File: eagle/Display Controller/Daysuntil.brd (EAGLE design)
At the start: 45 parts, among them IC1 DS1307, IC2 ATMEGA168-20P, IC3 74HC595N, IC4 74HC595N, IC5 7805TV, Q1 32.768 kHz, T1 BC337, T10 BC337, T11 BC337, T12 BC337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

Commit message: updated board config
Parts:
- C1, C4, C5, C6: value 10uF -> 0.1uF
- C2, C3: value 10uF -> 100uF
- U$2: value (none) -> 16MHz
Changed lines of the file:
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@@
 <attribute name="VALUE" x="66.9798" y="40.132" size="1.778" layer="27" ratio="10" rot="R90"/>
 </element>
-<element name="U$2" library="adafruit" package="CERM_OSC" value="" x="46.99" y="33.02" smashed="yes" rot="R180">
+<element name="U$2" library="adafruit" package="CERM_OSC" value="16MHz" x="46.99" y="33.02" smashed="yes" rot="R180">
 <attribute name="VALUE" x="50.49" y="37.52" size="1.27" layer="27" rot="R180"/>
 </element>
@@
 <attribute name="VALUE" x="27.94" y="26.67" size="1.27" layer="27" ratio="10" rot="R90"/>
 </element>
-<element name="C2" library="adafruit" package="C050-050X075" value="10uF" x="22.86" y="27.94" smashed="yes" rot="R270">
+<element name="C2" library="adafruit" package="C050-050X075" value="100uF" x="22.86" y="27.94" smashed="yes" rot="R270">
 <attribute name="NAME" x="22.479" y="23.749" size="1.27" layer="25" ratio="10" rot="R180"/>
 <attribute name="VALUE" x="20.701" y="31.115" size="1.27" layer="27" ratio="10" rot="R270"/>
 </element>
-<element name="C3" library="adafruit" package="C050-050X075" value="10uF" x="36.83" y="31.75" smashed="yes" rot="R90">
+<element name="C3" library="adafruit" package="C050-050X075" value="100uF" x="36.83" y="31.75" smashed="yes" rot="R90">
 <attribute name="NAME" x="37.719" y="27.559" size="1.27" layer="25" ratio="10" rot="R180"/>
 <attribute name="VALUE" x="38.989" y="28.575" size="1.27" layer="27" ratio="10" rot="R90"/>
 </element>
 <element name="JP1" library="pinhead" package="1X16" value="Output" x="17.78" y="46.99" rot="R270"/>
-<element name="C1" library="adafruit" package="C025-030X050" value="10uF" x="67.31" y="68.58" smashed="yes">
+<element name="C1" library="adafruit" package="C025-030X050" value="0.1uF" x="67.31" y="68.58" smashed="yes">
 <attribute name="NAME" x="66.294" y="70.485" size="1.27" layer="25" ratio="10"/>
 <attribute name="VALUE" x="65.024" y="65.532" size="1.27" layer="27" ratio="10"/>
 </element>
-<element name="C4" library="adafruit" package="C025-030X050" value="10uF" x="40.64" y="24.13" smashed="yes" rot="R270">
+<element name="C4" library="adafruit" package="C025-030X050" value="0.1uF" x="40.64" y="24.13" smashed="yes" rot="R270">
 <attribute name="NAME" x="39.624" y="27.305" size="1.27" layer="25" ratio="10"/>
 <attribute name="VALUE" x="38.354" y="19.812" size="1.27" layer="27" ratio="10"/>
 </element>
-<element name="C6" library="adafruit" package="C025-030X050" value="10uF" x="35.56" y="52.07" smashed="yes" rot="R90">
+<element name="C6" library="adafruit" package="C025-030X050" value="0.1uF" x="35.56" y="52.07" smashed="yes" rot="R90">
 <attribute name="NAME" x="38.735" y="48.514" size="1.27" layer="25" ratio="10" rot="R90"/>
 <attribute name="VALUE" x="38.608" y="52.324" size="1.27" layer="27" ratio="10" rot="R90"/>
 </element>
-<element name="C5" library="adafruit" package="C025-030X050" value="10uF" x="35.56" y="40.64" smashed="yes" rot="R90">
+<element name="C5" library="adafruit" package="C025-030X050" value="0.1uF" x="35.56" y="40.64" smashed="yes" rot="R90">
 <attribute name="NAME" x="38.735" y="37.084" size="1.27" layer="25" ratio="10" rot="R90"/>
 <attribute name="VALUE" x="38.608" y="40.894" size="1.27" layer="27" ratio="10" rot="R90"/>

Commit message: finalized board design
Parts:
- added SL1: (no value), con-amp-quick:02P
- IC2: value ATMEGA168-20P -> ATMEGA328P
- JP1: value Output -> (none); device pinhead:1X16 -> pinhead:1X14
- moved C1 66.2 mm to (40.0, 8.26), turned to 270 degrees
- moved IC2 60.8 mm to (19.7, 6.35), turned to 180 degrees
- moved R9 57.3 mm to (14.0, 31.1), turned to 180 degrees
- moved R8 52.0 mm to (14.0, 34.9), turned to 180 degrees
- moved R7 46.6 mm to (14.0, 38.7), turned to 180 degrees
- moved R6 41.3 mm to (14.0, 42.5), turned to 180 degrees
- moved R16 36.1 mm to (38.1, 31.1), turned to 180 degrees
- moved T6 36.0 mm to (8.26, 28.9), turned to 0 degrees
- moved R5 35.9 mm to (14.0, 46.4), turned to 180 degrees
- moved T4 32.6 mm to (8.26, 38.4), turned to 0 degrees
- moved T7 31.0 mm to (8.26, 25.4)
- moved R15 30.8 mm to (38.1, 34.9), turned to 180 degrees
- moved R4 30.6 mm to (14.0, 50.2), turned to 180 degrees
- moved T2 29.5 mm to (8.26, 47.9), turned to 0 degrees
- moved IC3 27.9 mm to (23.5, 41.9), turned to 270 degrees
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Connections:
- net +12V: now also SL1.2; no longer JP1.16
- net GND: now also SL1.1; no longer JP1.15
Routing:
- net N$7: track 0.00 -> 72.0 mm, vias 0 -> 1
- net N$6: track 0.00 -> 68.2 mm, vias 0 -> 1
- net N$2: track 0.00 -> 56.5 mm, vias 0 -> 1
- net 9: track 0.00 -> 55.1 mm, vias 0 -> 1
- net 8: track 0.00 -> 52.8 mm
- net 10: track 0.00 -> 49.1 mm
- net N$9: track 0.00 -> 48.7 mm, vias 0 -> 1
- net SER: track 0.00 -> 45.8 mm
- net 12: track 0.00 -> 42.1 mm, vias 0 -> 1
- net N$8: track 0.00 -> 41.0 mm
- net 11: track 0.00 -> 39.2 mm, vias 0 -> 1
- net 14: track 0.00 -> 33.7 mm
- net 13: track 0.00 -> 32.6 mm
- net SCL: track 0.00 -> 30.7 mm, vias 0 -> 1
- net SDA: track 0.00 -> 30.1 mm
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- added copper zone on layer 1, net GND
- added copper zone on layer 16, net VCC
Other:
- board outline added: 56.5 x 59.7 mm
- board text added: "/home/brian/Pictures/Images/santa1.bmp"
- board text added: "1"
- board text added: "RTC Display v1.0"
- board text added: "wilsonb@outlook.com"
- board text removed: "2.2K"
- board text removed: "4.7K"
- board text removed: "BC337"

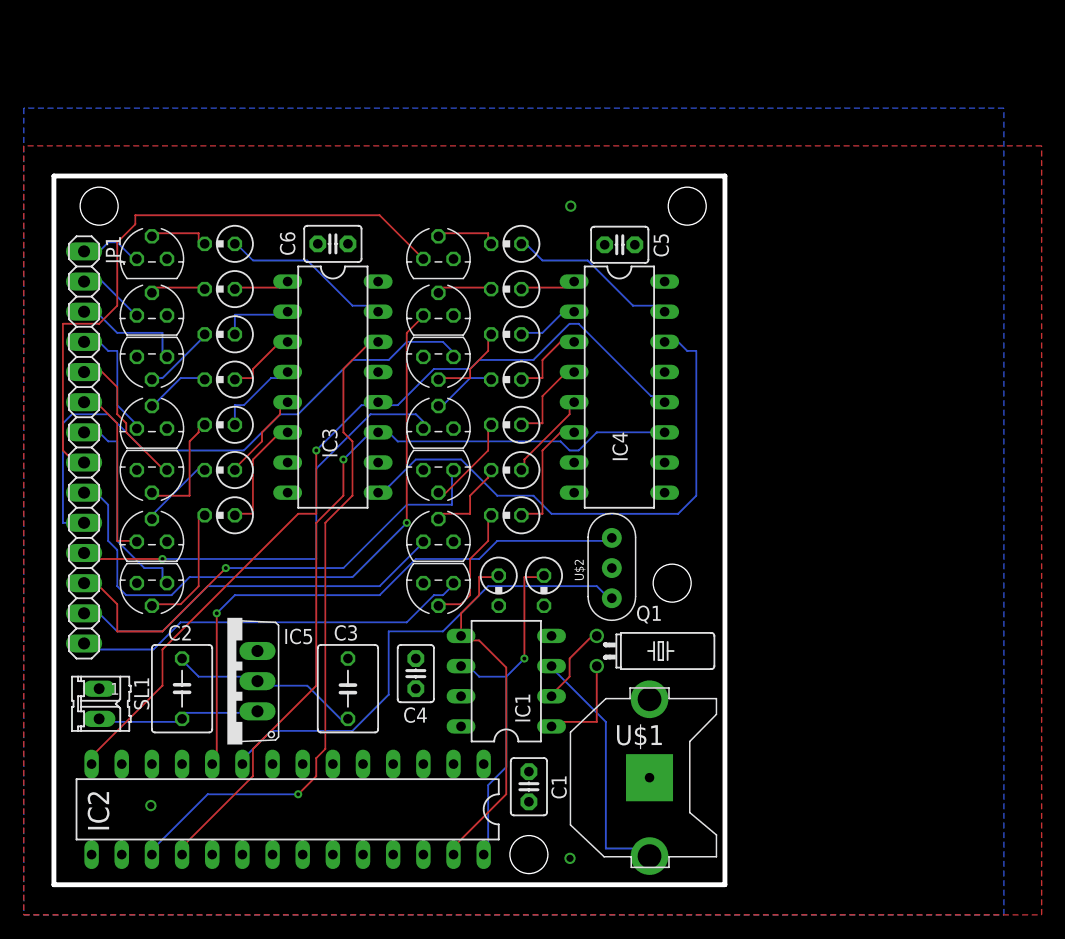
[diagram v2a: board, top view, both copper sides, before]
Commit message: final board design with CAM files
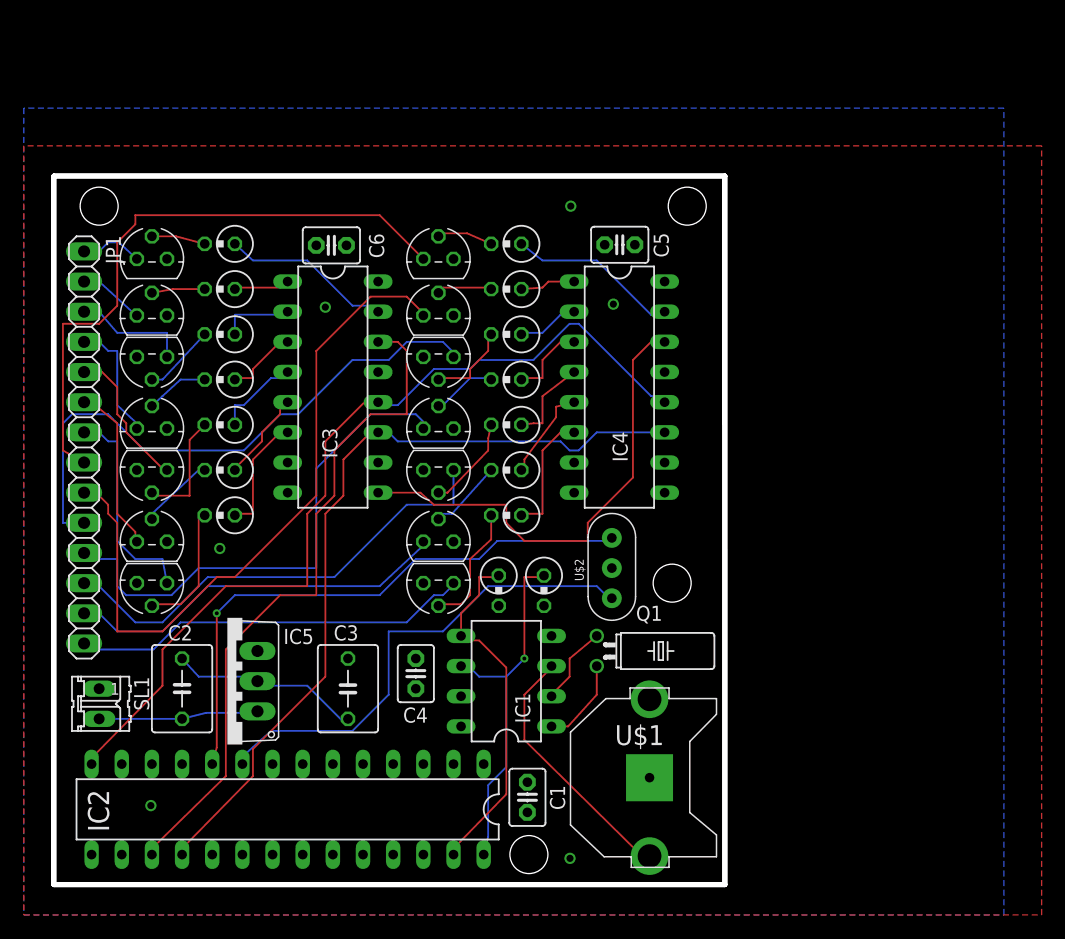
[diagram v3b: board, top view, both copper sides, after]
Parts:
- added U$3: (no value), bitmap:BITMAP-SLEIGHT
- moved C1 0.90 mm to (39.9, 7.37)
- moved C6 0.18 mm to (23.4, 53.8), turned to 180 degrees
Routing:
- net SER: track 45.8 -> 40.3 mm
- net 11: track 39.2 -> 43.5 mm, vias 1 -> 0
- net 9: track 55.1 -> 59.4 mm, vias 1 -> 0
- net N$7: track 72.0 -> 75.4 mm, vias 1 -> 0
- net 12: track 42.1 -> 39.5 mm, vias 1 -> 0
- net N$4: track 8.89 -> 7.41 mm
- net 6: track 15.5 -> 14.1 mm
- net N$21: track 7.60 -> 6.29 mm
- net N$2: track 56.5 -> 57.6 mm, vias 1 -> 0
- net +12V: track 14.4 -> 13.4 mm
- net N$1: track 5.38 -> 4.53 mm
- net 8: track 52.8 -> 52.1 mm
- net N$5: track 7.42 -> 6.78 mm
- net N$16: track 5.31 -> 4.71 mm
- net N$20: track 8.42 -> 7.89 mm
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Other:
- board text removed: "/home/brian/Pictures/Images/santa1.bmp"

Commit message: upload code v1 and fix ground on 7805 in board schematic.
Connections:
- removed net N$23: C2.2, C3.2, IC5.2
- net GND: now also C2.2, C3.2, IC5.2
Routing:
- net N$23: track 16.3 -> 0.00 mm
- net GND: track 0.00 -> 16.3 mm
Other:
- board text added: "RTC Display v1.1"
- board text removed: "RTC Display v1.0"
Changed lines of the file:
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@@
 <wire x1="56.515" y1="59.69" x2="56.515" y2="0" width="0.4064" layer="20"/>
 <hole x="3.81" y="57.15" drill="3.2"/>
-<text x="16.4338" y="56.5277" size="1.778" layer="121" font="vector">RTC Display v1.0</text>
+<text x="16.4338" y="56.5277" size="1.778" layer="121" font="vector">RTC Display v1.1</text>
 <text x="55.3212" y="27.305" size="1.778" layer="121" font="vector" rot="R90">wilsonb@outlook.com</text>
 <wire x1="0" y1="0" x2="0" y2="59.69" width="0.4064" layer="20"/>
@@
 <vertex x="83.185" y="62.23"/>
 </polygon>
+<contactref element="C2" pad="2"/>
+<contactref element="IC5" pad="2"/>
+<contactref element="C3" pad="2"/>
+<wire x1="12.192" y1="17.526" x2="10.795" y2="19.05" width="0.1524" layer="16"/>
+<wire x1="16.764" y1="17.526" x2="12.192" y2="17.526" width="0.1524" layer="16"/>
+<wire x1="16.764" y1="17.526" x2="17.145" y2="17.145" width="0.1524" layer="16"/>
+<wire x1="21.336" y1="16.764" x2="24.384" y2="13.716" width="0.1524" layer="16"/>
+<wire x1="17.526" y1="16.764" x2="21.336" y2="16.764" width="0.1524" layer="16"/>
+<wire x1="24.384" y1="13.716" x2="24.765" y2="13.97" width="0.1524" layer="16"/>
+<wire x1="17.526" y1="16.764" x2="17.145" y2="17.145" width="0.1524" layer="16"/>
 </signal>
 <signal name="VCC">
@@
 <wire x1="10.795" y1="13.97" x2="3.81" y2="13.97" width="0.1524" layer="16"/>
 </signal>
-<signal name="N$23">
-<contactref element="C2" pad="2"/>
-<contactref element="IC5" pad="2"/>
-<contactref element="C3" pad="2"/>
-<wire x1="12.192" y1="17.526" x2="10.795" y2="19.05" width="0.1524" layer="16"/>
-<wire x1="16.764" y1="17.526" x2="12.192" y2="17.526" width="0.1524" layer="16"/>
-<wire x1="16.764" y1="17.526" x2="17.145" y2="17.145" width="0.1524" layer="16"/>
-<wire x1="21.336" y1="16.764" x2="24.384" y2="13.716" width="0.1524" layer="16"/>
-<wire x1="17.526" y1="16.764" x2="21.336" y2="16.764" width="0.1524" layer="16"/>
-<wire x1="24.384" y1="13.716" x2="24.765" y2="13.97" width="0.1524" layer="16"/>
-<wire x1="17.526" y1="16.764" x2="17.145" y2="17.145" width="0.1524" layer="16"/>
-</signal>
 <signal name="1">
